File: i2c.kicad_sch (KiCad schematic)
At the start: 42 parts, among them J12 JST_SH_1x4_BM04B-SRSS-TB-LF-SN, Q21 BSS84AKW, Q23 BSS84AKW, U23 TS5A3359_VSSOP, U24 TS5A3359_VSSOP, U33 TPD4E05U06QDQARQ1, U45 PCA9517ADP, U49 TCA39306_VSSOP

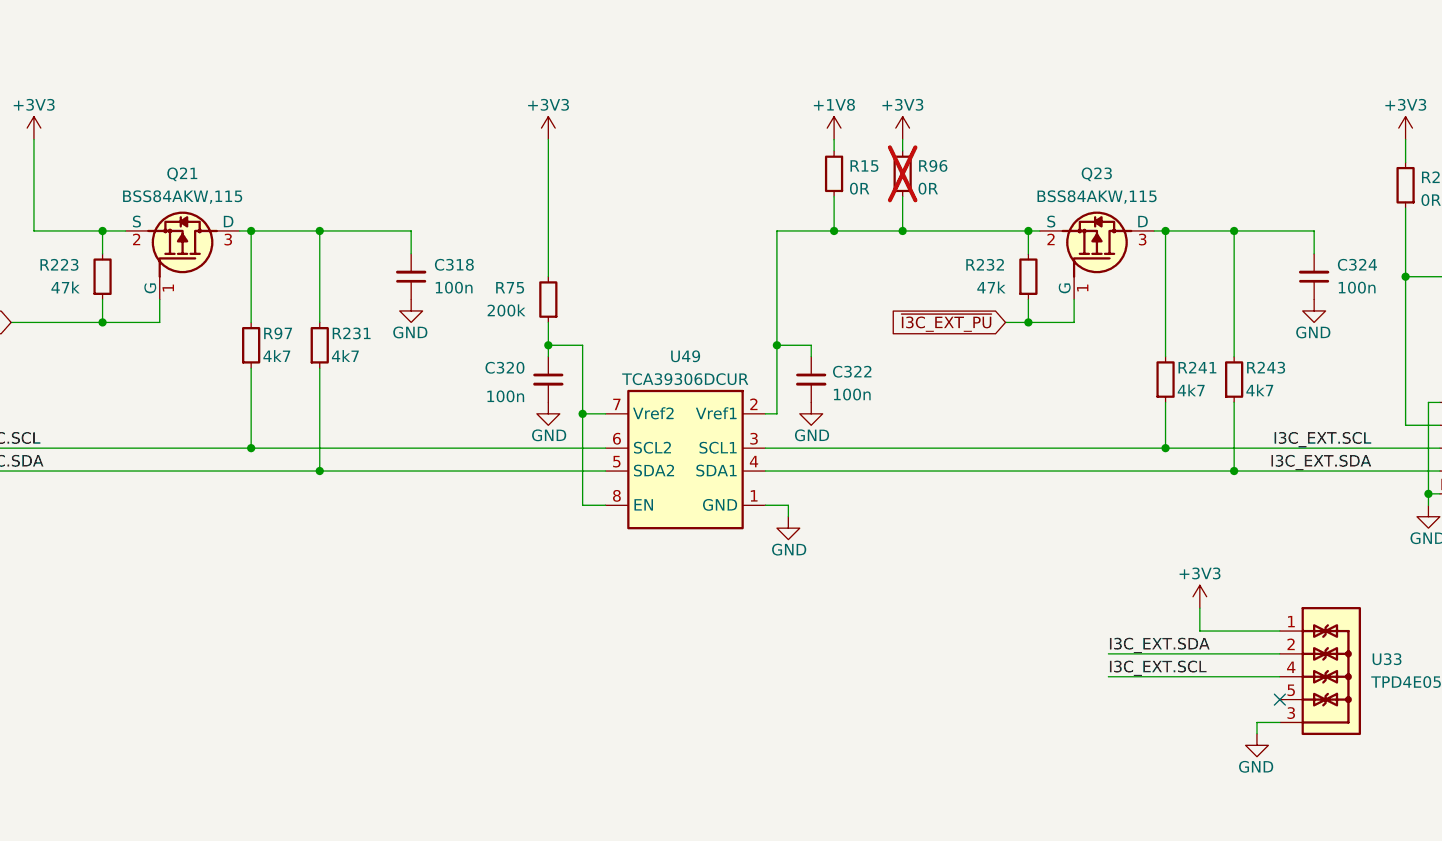
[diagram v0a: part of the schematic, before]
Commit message: [#67408] Update layout for I3C, SDcard and HDMI aux signals
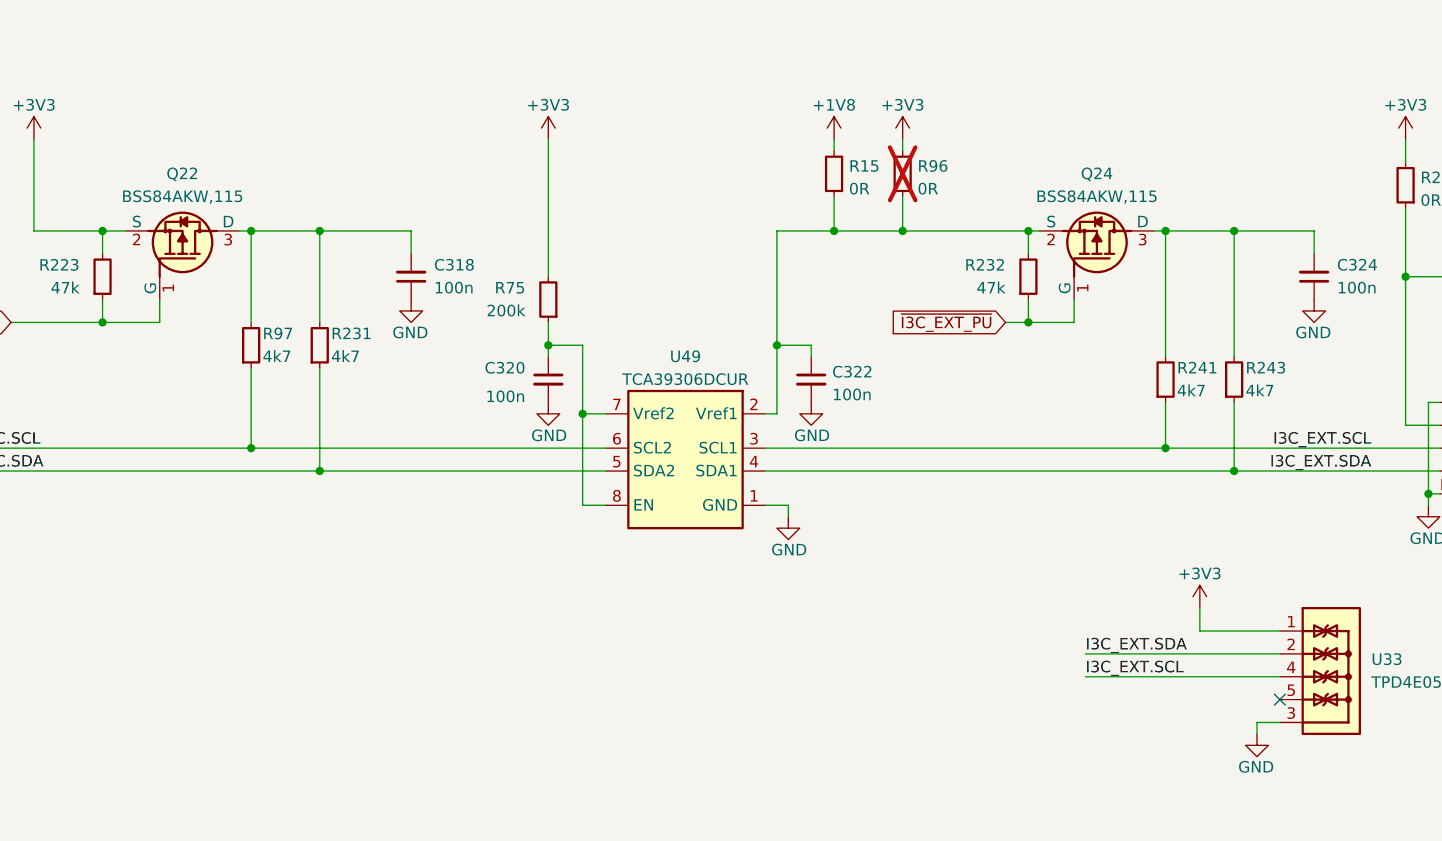
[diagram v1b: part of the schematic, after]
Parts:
- renumbered Q21 to Q22, Q23 to Q24
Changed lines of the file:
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@@
     (stroke (width 0) (type default))
   )
-  (wire (pts (xy 334.01 110.49) (xy 353.06 110.49))
+  (wire (pts (xy 331.47 110.49) (xy 353.06 110.49))
     (stroke (width 0) (type default))
   )
@@
     (stroke (width 0) (type default))
   )
-  (wire (pts (xy 334.01 107.95) (xy 353.06 107.95))
+  (wire (pts (xy 331.47 107.95) (xy 353.06 107.95))
     (stroke (width 0) (type default))
   )
@@
     (effects (font (size 1.27 1.27)) (justify left bottom))
   )
-  (label "I3C_EXT.SCL" (at 334.01 110.49 0) (fields_autoplaced)
+  (label "I3C_EXT.SCL" (at 331.47 110.49 0) (fields_autoplaced)
     (effects (font (size 1.27 1.27)) (justify left bottom))
   )
@@
     (effects (font (size 1.27 1.27)) (justify right bottom))
   )
-  (label "I3C_EXT.SDA" (at 334.01 107.95 0) (fields_autoplaced)
+  (label "I3C_EXT.SDA" (at 331.47 107.95 0) (fields_autoplaced)
     (effects (font (size 1.27 1.27)) (justify left bottom))
   )
@@
   (symbol (lib_id "antmicroTransistorsFETsMOSFETsSingle:BSS84AKW") (at 228.6 68.58 270) (mirror x) (unit 1)
     (in_bom yes) (on_board yes) (dnp no)
-    (property "Reference" "Q21" (at 231.14 54.61 90)
+    (property "Reference" "Q22" (at 231.14 54.61 90)
       (effects (font (size 1.27 1.27) (thickness 0.15)))
     )
@@
       (project "data-center-rdimm-ddr5-tester"
         (path "/1faa6543-e26a-4449-8bac-ee14b9f19e5f/3f0d6799-172b-44a7-b59e-98d6f5f3049b"
-          (reference "Q21") (unit 1)
+          (reference "Q22") (unit 1)
         )
       )
@@
   (symbol (lib_id "antmicroTransistorsFETsMOSFETsSingle:BSS84AKW") (at 330.2 68.58 270) (mirror x) (unit 1)
     (in_bom yes) (on_board yes) (dnp no)
-    (property "Reference" "Q23" (at 332.74 54.61 90)
+    (property "Reference" "Q24" (at 332.74 54.61 90)
       (effects (font (size 1.27 1.27) (thickness 0.15)))
     )
@@
       (project "data-center-rdimm-ddr5-tester"
         (path "/1faa6543-e26a-4449-8bac-ee14b9f19e5f/3f0d6799-172b-44a7-b59e-98d6f5f3049b"
-          (reference "Q23") (unit 1)
+          (reference "Q24") (unit 1)
         )
       )

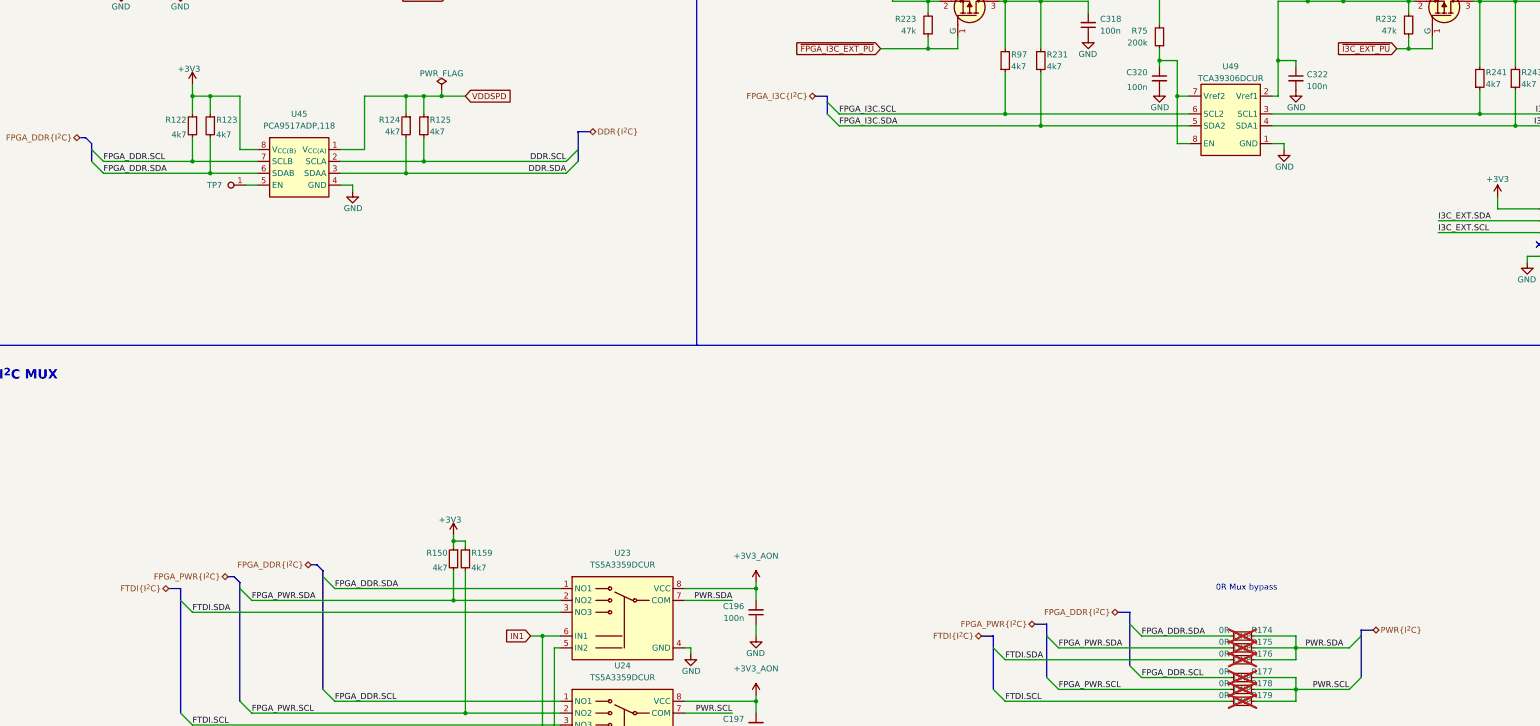
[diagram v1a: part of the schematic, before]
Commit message: [#68016] Improve bus entry marking
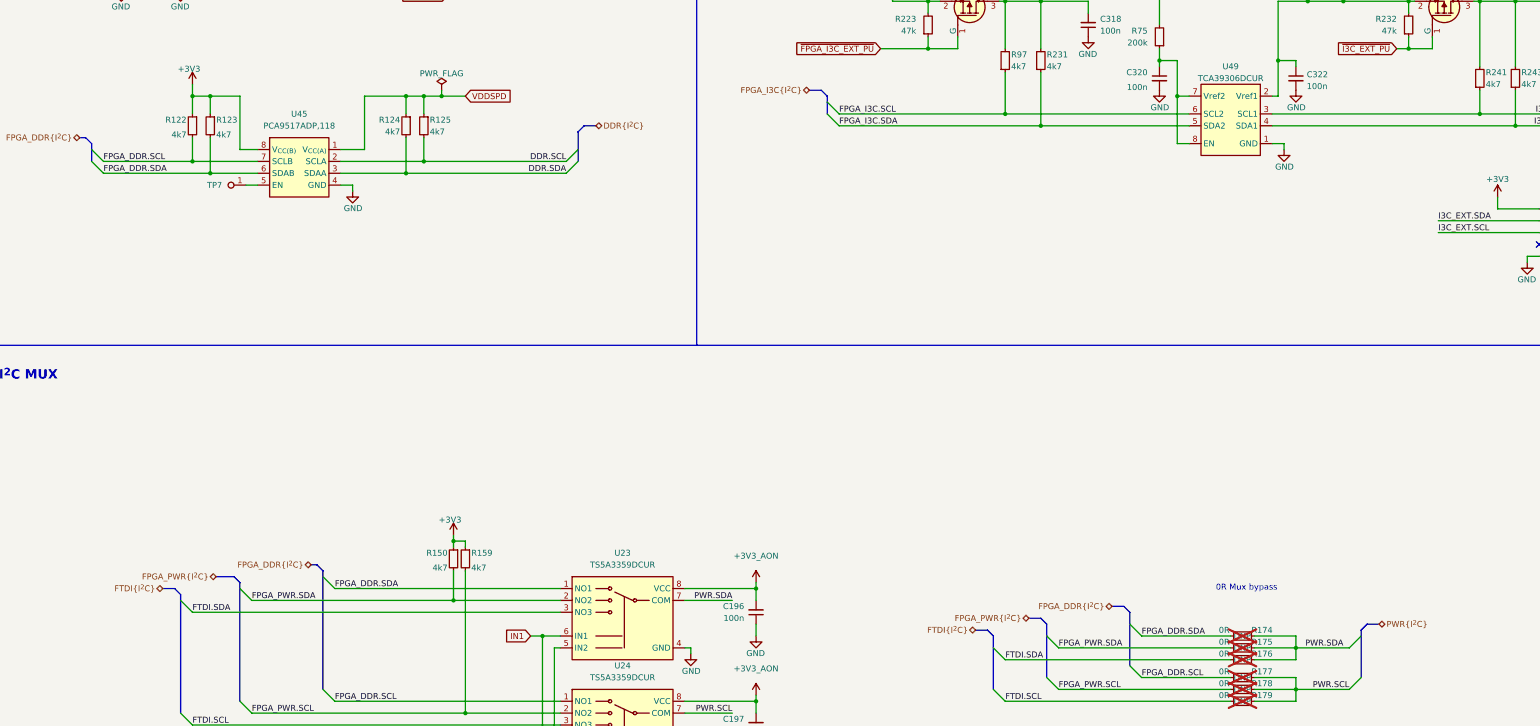
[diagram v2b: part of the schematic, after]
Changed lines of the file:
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@@
+    (stroke (width 0) (type default))
+  )
+  (bus (pts (xy 246.38 193.04) (xy 247.65 194.31))
     (stroke (width 0) (type default))
   )
@@
     (stroke (width 0) (type default))
   )
-  (bus (pts (xy 72.39 184.15) (xy 73.66 184.15))
+  (bus (pts (xy 69.85 184.15) (xy 73.66 184.15))
     (stroke (width 0) (type default))
   )
@@
     (stroke (width 0) (type default))
   )
-  (bus (pts (xy 149.86 88.9) (xy 147.32 88.9))
+  (bus (pts (xy 151.13 87.63) (xy 148.59 87.63))
     (stroke (width 0) (type default))
   )
@@
     (stroke (width 0) (type default))
   )
-  (bus (pts (xy 62.23 186.69) (xy 62.23 189.23))
+  (bus (pts (xy 62.23 187.96) (xy 62.23 189.23))
     (stroke (width 0) (type default))
   )
@@
     (stroke (width 0) (type default))
   )
+  (bus (pts (xy 200.66 81.28) (xy 199.39 80.01))
+    (stroke (width 0) (type default))
+  )
   (wire (pts (xy 295.91 85.09) (xy 340.36 85.09))
     (stroke (width 0) (type default))
   )
+  (bus (pts (xy 234.95 195.58) (xy 236.22 196.85))
+    (stroke (width 0) (type default))
+  )
   (wire (pts (xy 64.77 81.28) (xy 64.77 85.09))
     (stroke (width 0) (type default))
@@
     (stroke (width 0) (type default))
   )
+  (bus (pts (xy 60.96 186.69) (xy 62.23 187.96))
+    (stroke (width 0) (type default))
+  )
   (wire (pts (xy 275.59 73.66) (xy 275.59 81.28))
     (stroke (width 0) (type default))
@@
     (stroke (width 0) (type default))
   )
-  (bus (pts (xy 317.5 195.58) (xy 314.96 195.58))
+  (bus (pts (xy 318.77 194.31) (xy 316.23 194.31))
     (stroke (width 0) (type default))
   )
@@
     (stroke (width 0) (type default))
   )
-  (bus (pts (xy 198.12 81.28) (xy 200.66 81.28))
+  (bus (pts (xy 196.85 80.01) (xy 199.39 80.01))
     (stroke (width 0) (type default))
   )
@@
     (stroke (width 0) (type default))
   )
+  (bus (pts (xy 316.23 194.31) (xy 314.96 195.58))
+    (stroke (width 0) (type default))
+  )
   (wire (pts (xy 246.38 76.2) (xy 246.38 87.63))
     (stroke (width 0) (type default))
@@
     (stroke (width 0) (type default))
   )
-  (bus (pts (xy 59.69 186.69) (xy 62.23 186.69))
+  (bus (pts (xy 58.42 186.69) (xy 60.96 186.69))
     (stroke (width 0) (type default))
   )
@@
     (stroke (width 0) (type default))
   )
-  (bus (pts (xy 245.11 194.31) (xy 247.65 194.31))
+  (bus (pts (xy 243.84 193.04) (xy 246.38 193.04))
     (stroke (width 0) (type default))
   )
@@
     (stroke (width 0) (type default))
   )
-  (bus (pts (xy 233.68 196.85) (xy 236.22 196.85))
+  (bus (pts (xy 232.41 195.58) (xy 234.95 195.58))
     (stroke (width 0) (type default))
   )
@@
     (stroke (width 0) (type default))
   )
+  (bus (pts (xy 264.16 190.5) (xy 265.43 191.77))
+    (stroke (width 0) (type default))
+  )
   (wire (pts (xy 120.65 182.88) (xy 120.65 189.23))
     (stroke (width 0) (type default))
@@
     (stroke (width 0) (type default))
   )
-  (bus (pts (xy 262.89 191.77) (xy 265.43 191.77))
+  (bus (pts (xy 261.62 190.5) (xy 264.16 190.5))
     (stroke (width 0) (type default))
   )
@@
   )
   (bus (pts (xy 40.64 90.17) (xy 41.91 90.17))
+    (stroke (width 0) (type default))
+  )
+  (bus (pts (xy 147.32 88.9) (xy 148.59 87.63))
     (stroke (width 0) (type default))
   )
@@
     (effects (font (size 1.27 1.27)) (justify right))
   )
-  (hierarchical_label "PWR{I^{2}C}" (shape bidirectional) (at 317.5 195.58 0) (fields_autoplaced)
+  (hierarchical_label "PWR{I^{2}C}" (shape bidirectional) (at 318.77 194.31 0) (fields_autoplaced)
     (effects (font (size 1.27 1.27)) (justify left))
   )
-  (hierarchical_label "DDR{I^{2}C}" (shape bidirectional) (at 149.86 88.9 0) (fields_autoplaced)
+  (hierarchical_label "DDR{I^{2}C}" (shape bidirectional) (at 151.13 87.63 0) (fields_autoplaced)
     (effects (font (size 1.27 1.27)) (justify left))
   )
-  (hierarchical_label "FTDI{I^{2}C}" (shape bidirectional) (at 233.68 196.85 180) (fields_autoplaced)
+  (hierarchical_label "FTDI{I^{2}C}" (shape bidirectional) (at 232.41 195.58 180) (fields_autoplaced)
     (effects (font (size 1.27 1.27)) (justify right))
   )
@@
     (effects (font (size 1.27 1.27)) (justify right))
   )
-  (hierarchical_label "FPGA_PWR{I^{2}C}" (shape bidirectional) (at 72.39 184.15 180) (fields_autoplaced)
-    (effects (font (size 1.27 1.27)) (justify right))
-  )
-  (hierarchical_label "FTDI{I^{2}C}" (shape bidirectional) (at 59.69 186.69 180) (fields_autoplaced)
-    (effects (font (size 1.27 1.27)) (justify right))
-  )
-  (hierarchical_label "FPGA_DDR{I^{2}C}" (shape bidirectional) (at 262.89 191.77 180) (fields_autoplaced)
-    (effects (font (size 1.27 1.27)) (justify right))
-  )
-  (hierarchical_label "FPGA_PWR{I^{2}C}" (shape bidirectional) (at 245.11 194.31 180) (fields_autoplaced)
-    (effects (font (size 1.27 1.27)) (justify right))
-  )
-  (hierarchical_label "FPGA_I3C{I^{2}C}" (shape bidirectional) (at 198.12 81.28 180) (fields_autoplaced)
-    (effects (font (size 1.27 1.27)) (justify right))
-  )
+  (hierarchical_label "FPGA_PWR{I^{2}C}" (shape bidirectional) (at 69.85 184.15 180) (fields_autoplaced)
+    (effects (font (size 1.27 1.27)) (justify right))
+  )
+  (hierarchical_label "FTDI{I^{2}C}" (shape bidirectional) (at 58.42 186.69 180) (fields_autoplaced)
+    (effects (font (size 1.27 1.27)) (justify right))
+  )
+  (hierarchical_label "FPGA_DDR{I^{2}C}" (shape bidirectional) (at 261.62 190.5 180) (fields_autoplaced)
+    (effects (font (size 1.27 1.27)) (justify right))
+  )
+  (hierarchical_label "FPGA_PWR{I^{2}C}" (shape bidirectional) (at 243.84 193.04 180) (fields_autoplaced)
+    (effects (font (size 1.27 1.27)) (justify right))
+  )
+  (hierarchical_label "FPGA_I3C{I^{2}C}" (shape bidirectional) (at 196.85 80.01 180) (fields_autoplaced)
+    (effects (font (size 1.27 1.27)) (justify right))
+  )

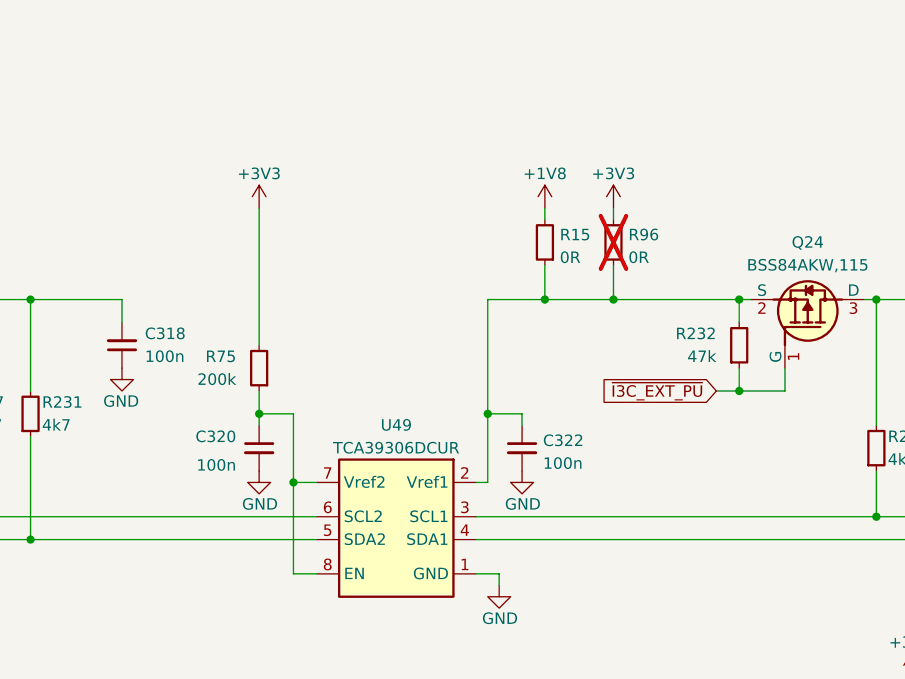
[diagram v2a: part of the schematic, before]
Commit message: [#68016] Solve ERC warrings and errors
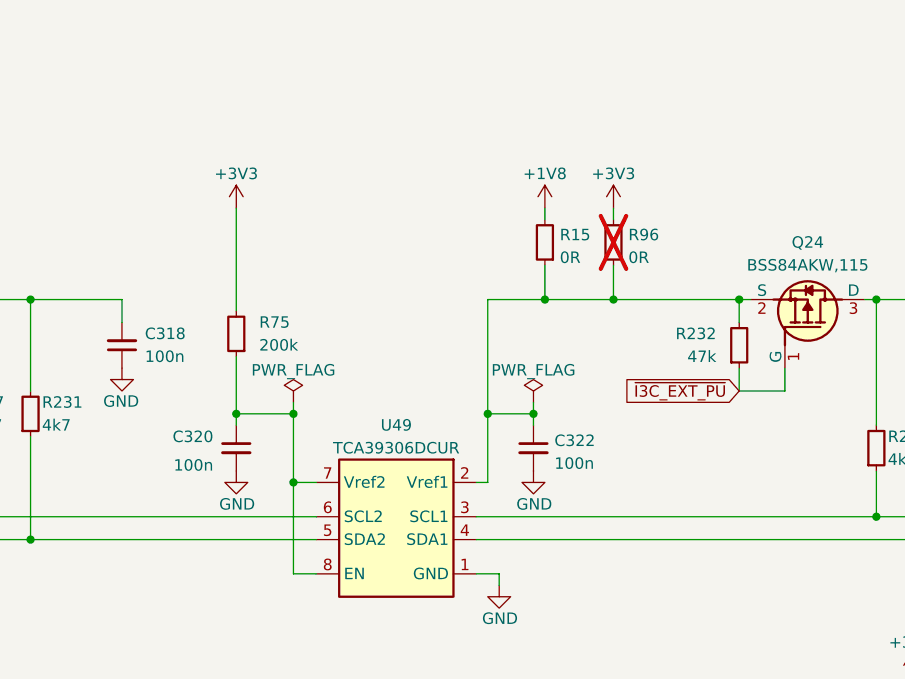
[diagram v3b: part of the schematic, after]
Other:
- moved on the sheet: C320, C322, R75
